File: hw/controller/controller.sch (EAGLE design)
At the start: 103 parts, among them J1 XT30XT30PW_MALE, J2 XT30XT30PW_MALE, M1 MOUNT, M2 MOUNT, M3 MOUNT, M4 MOUNT, Q1 TPH1R204PLSOP_ADVANCE_8, Q2 TPH1R204PLSOP_ADVANCE_8, Q3 TPH1R204PLSOP_ADVANCE_8, Q4 TPH1R204PLSOP_ADVANCE_8, Q5 TPH1R204PLSOP_ADVANCE_8, Q6 TPH1R204PLSOP_ADVANCE_8, U1 STM32G474CEU6, U2 TCAN334GSOT23, U3 AS5147, U4 DRV8323RS

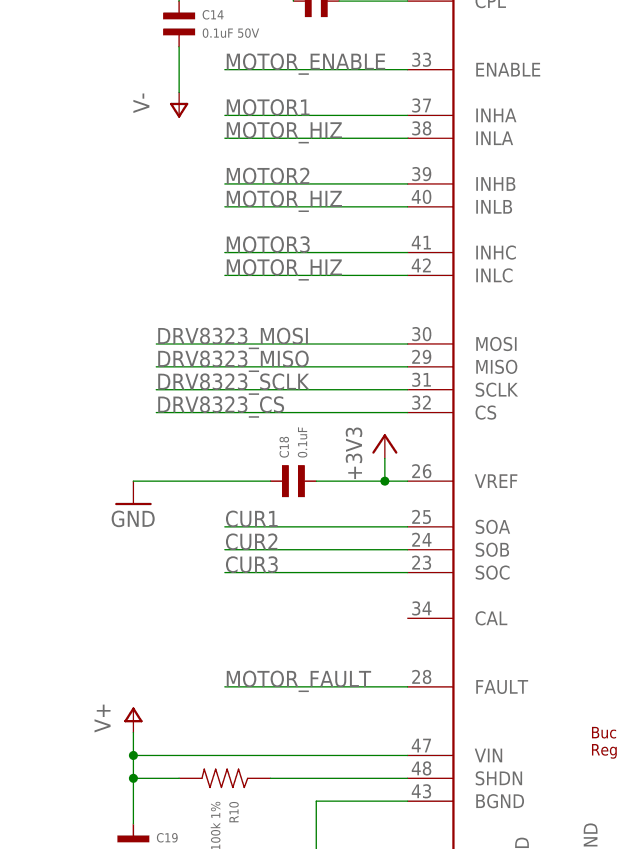
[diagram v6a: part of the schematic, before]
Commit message: Minor tweaks for a r4.2 moteus controller
 * Add two pullups
 * Tweak some silk
 * Update the version number on board and schematic
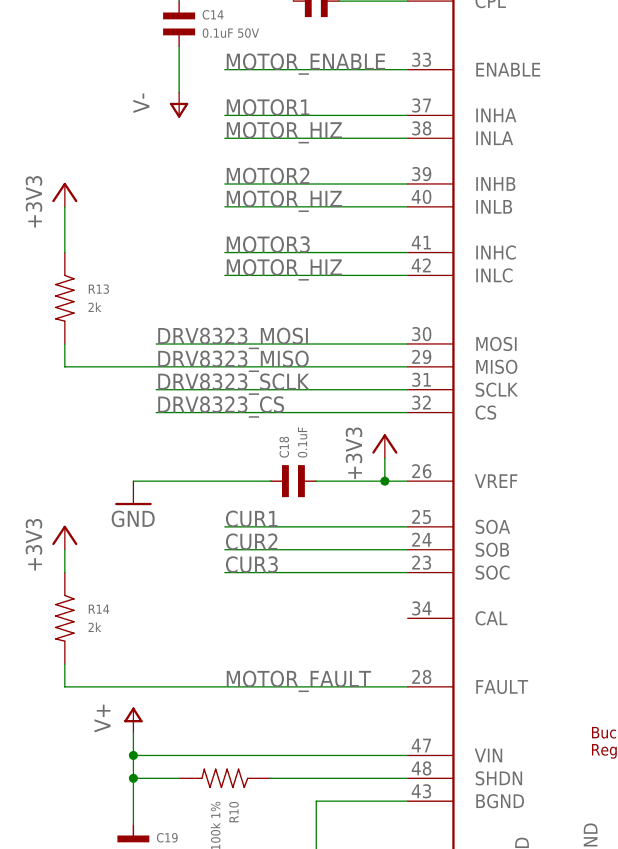
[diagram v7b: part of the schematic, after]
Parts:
- added R13, R14: 2k, mfpassives:RESISTOR_0402
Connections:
- net +3V3: now also R13.P$1, R14.P$1
- net DRV8323_MISO: now also R13.P$2
- net MOTOR_FAULT: now also R14.P$2
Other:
- note added: "moteus r4.2 (c) jjp@pobox.com 2019 Licensed under the Apache 2.0 License"
- note removed: "moteus r4.1 (c) jjp@pobox.com 2019 Licensed under the Apache 2.0 License"
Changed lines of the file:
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@@
 <part name="+3V13" library="supply1" deviceset="+3V3" device=""/>
 <part name="+3V14" library="supply1" deviceset="+3V3" device=""/>
+<part name="R13" library="mfpassives" deviceset="RESISTOR" device="_0402" value="2k">
+<attribute name="HOUSEPART" value="YES"/>
+<attribute name="MF" value=""/>
+<attribute name="MPN" value="MF-RES-0402-2K"/>
+</part>
+<part name="+3V15" library="supply1" deviceset="+3V3" device=""/>
+<part name="R14" library="mfpassives" deviceset="RESISTOR" device="_0402" value="2k">
+<attribute name="HOUSEPART" value="YES"/>
+<attribute name="MF" value=""/>
+<attribute name="MPN" value="MF-RES-0402-2K"/>
+</part>
+<part name="+3V16" library="supply1" deviceset="+3V3" device=""/>
 </parts>
 <sheets>
@@
 <text x="-132.08" y="-142.24" size="5.08" layer="90">POWER FETS</text>
 <text x="73.66" y="-142.24" size="5.08" layer="90">BULK CAPACITANCE</text>
-<text x="-307.34" y="200.66" size="7.62" layer="90">moteus r4.1
+<text x="-307.34" y="200.66" size="7.62" layer="90">moteus r4.2
 (c) jjp@pobox.com 2019
 Licensed under the Apache 2.0 License</text>
@@
 <instance part="+3V13" gate="G$1" x="157.48" y="190.5"/>
 <instance part="+3V14" gate="G$1" x="-71.12" y="129.54"/>
+<instance part="R13" gate="G$1" x="-289.56" y="-208.28">
+<attribute name="MPN" x="-289.56" y="-208.28" size="1.778" layer="96" display="off"/>
+<attribute name="MF" x="-289.56" y="-208.28" size="1.778" layer="96" display="off"/>
+</instance>
+<instance part="+3V15" gate="G$1" x="-289.56" y="-195.58"/>
+<instance part="R14" gate="G$1" x="-289.56" y="-243.84">
+<attribute name="MPN" x="-289.56" y="-243.84" size="1.778" layer="96" display="off"/>
+<attribute name="MF" x="-289.56" y="-243.84" size="1.778" layer="96" display="off"/>
+</instance>
+<instance part="+3V16" gate="G$1" x="-289.56" y="-233.68"/>
 </instances>
 <busses>
@@
 <wire x1="-71.12" y1="121.92" x2="-68.58" y2="121.92" width="0.1524" layer="91"/>
 </segment>
+<segment>
+<pinref part="R13" gate="G$1" pin="P$1"/>
+<pinref part="+3V15" gate="G$1" pin="+3V3"/>
+<wire x1="-289.56" y1="-203.2" x2="-289.56" y2="-198.12" width="0.1524" layer="91"/>
+</segment>
+<segment>
+<pinref part="R14" gate="G$1" pin="P$1"/>
+<pinref part="+3V16" gate="G$1" pin="+3V3"/>
+<wire x1="-289.56" y1="-238.76" x2="-289.56" y2="-236.22" width="0.1524" layer="91"/>
+</segment>
 </net>
 <net name="GND" class="0">
@@
 <segment>
 <pinref part="U4" gate="G$1" pin="MISO"/>
-<wire x1="-279.4" y1="-215.9" x2="-251.46" y2="-215.9" width="0.1524" layer="91"/>
+<wire x1="-289.56" y1="-215.9" x2="-251.46" y2="-215.9" width="0.1524" layer="91"/>
 <label x="-279.4" y="-215.9" size="1.778" layer="95"/>
+<pinref part="R13" gate="G$1" pin="P$2"/>
+<wire x1="-289.56" y1="-215.9" x2="-289.56" y2="-213.36" width="0.1524" layer="91"/>
 </segment>
 <segment>
@@
 <segment>
 <pinref part="U4" gate="G$1" pin="FAULT"/>
-<wire x1="-251.46" y1="-251.46" x2="-271.78" y2="-251.46" width="0.1524" layer="91"/>
+<wire x1="-251.46" y1="-251.46" x2="-289.56" y2="-251.46" width="0.1524" layer="91"/>
 <label x="-271.78" y="-251.46" size="1.778" layer="95"/>
-</segment>
-<segment>
+<pinref part="R14" gate="G$1" pin="P$2"/>
+<wire x1="-289.56" y1="-251.46" x2="-289.56" y2="-248.92" width="0.1524" layer="91"/>
+</segment>
+<segment>

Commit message: Start on r4.3 with updated silk and moved phase outputs
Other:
- note added: "moteus r4.3 (c) jjp@pobox.com 2019 Licensed under the Apache 2.0 License"
- note removed: "moteus r4.2 (c) jjp@pobox.com 2019 Licensed under the Apache 2.0 License"
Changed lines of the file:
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@@
 <text x="-132.08" y="-142.24" size="5.08" layer="90">POWER FETS</text>
 <text x="73.66" y="-142.24" size="5.08" layer="90">BULK CAPACITANCE</text>
-<text x="-307.34" y="200.66" size="7.62" layer="90">moteus r4.2
+<text x="-307.34" y="200.66" size="7.62" layer="90">moteus r4.3
 (c) jjp@pobox.com 2019
 Licensed under the Apache 2.0 License</text>
